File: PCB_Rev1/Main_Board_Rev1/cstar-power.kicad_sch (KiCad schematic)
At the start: 49 parts, among them IC1 LT8648SEV#PBF, J4 Conn_01x02_Pin, J5 XT60PW-M, J6 Conn_01x02_Pin, J7 Conn_01x02_Pin, J8 Conn_01x02_Pin, U1 AZ1117IH-3.3TRG1

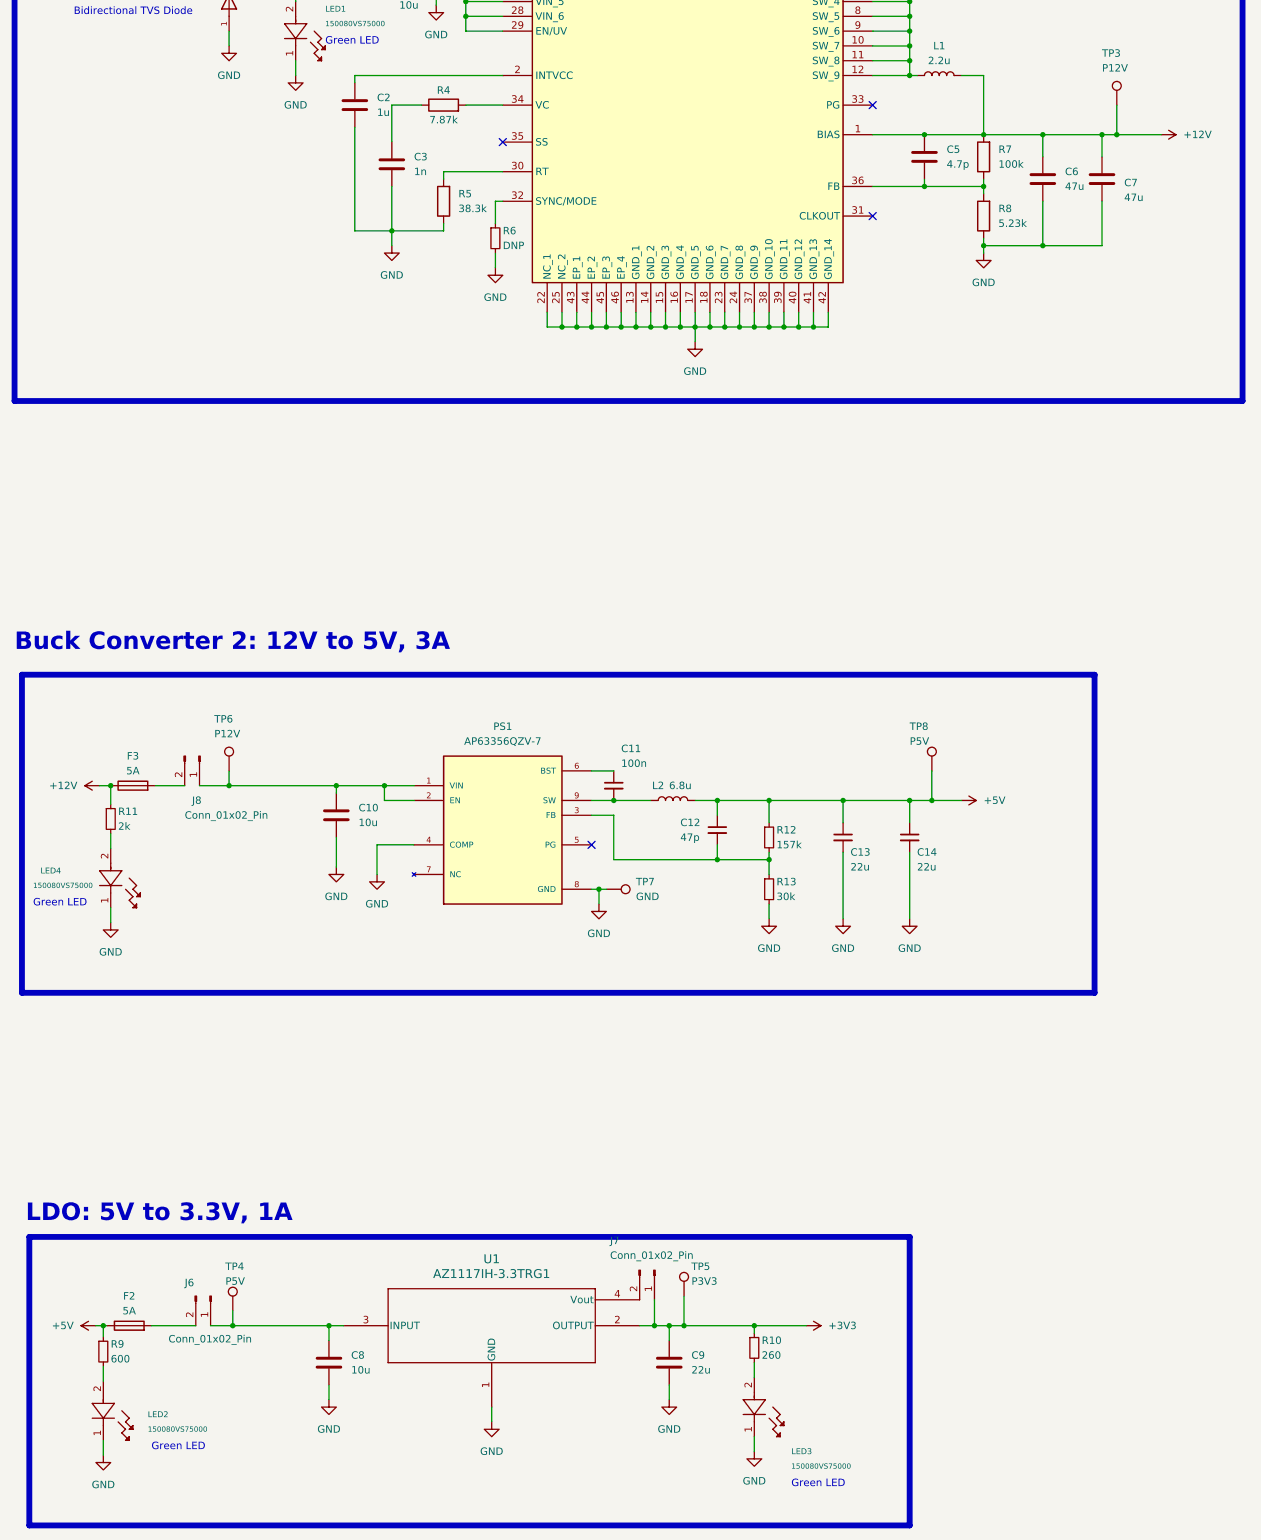
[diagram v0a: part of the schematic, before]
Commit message: schem changes made in BMS
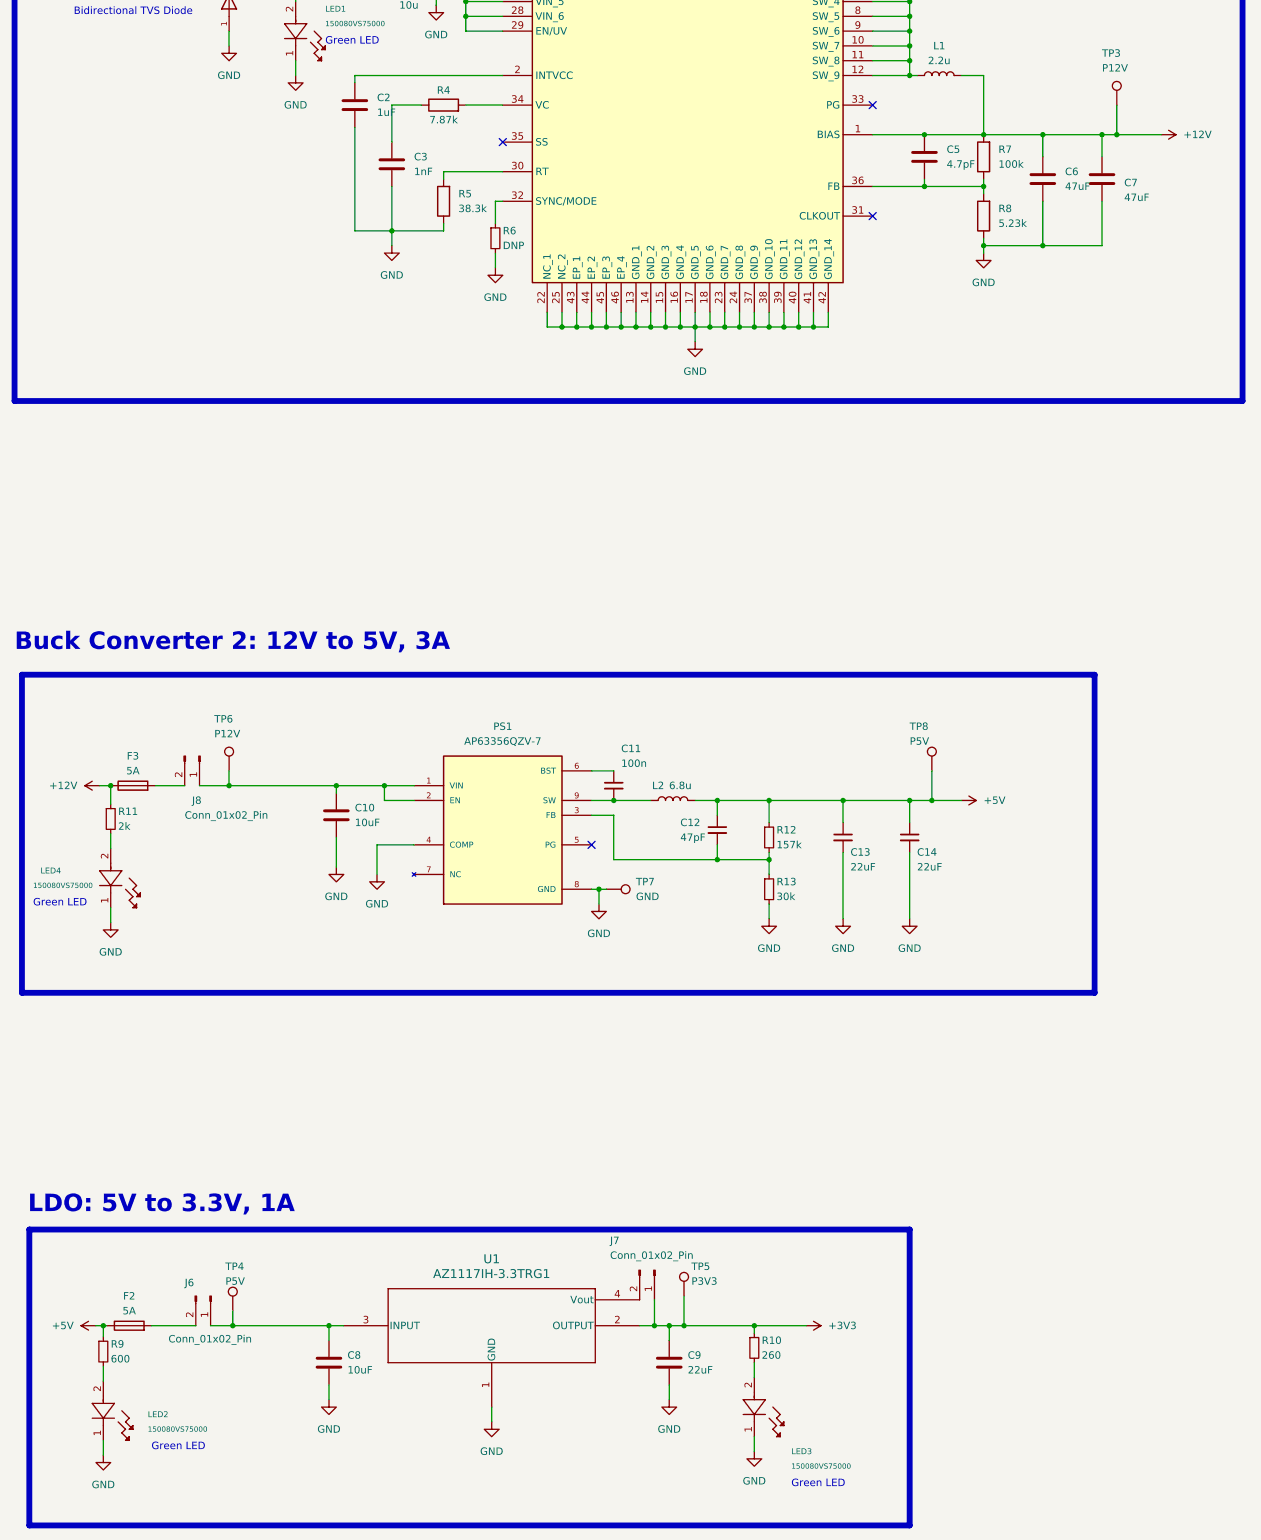
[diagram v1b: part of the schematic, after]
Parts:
- C10, C8: value 10u -> 10uF
- C12: value 47p -> 47pF
- C13, C14, C9: value 22u -> 22uF
- C2: value 1u -> 1uF
- C3: value 1n -> 1nF
- C5: value 4.7p -> 4.7pF
- C6, C7: value 47u -> 47uF
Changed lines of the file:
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@@
 	)
 	(rectangle
-		(start 45.72 292.1)
+		(start 45.72 290.83)
 		(end 196.85 341.63)
 		(stroke
@@
 	(text "LDO: 5V to 3.3V, 1A\n\n"
 		(exclude_from_sim no)
-		(at 45.085 294.64 0)
+		(at 45.466 293.116 0)
 		(effects
 			(font
@@
 			)
 		)
-		(property "Value" "47u"
+		(property "Value" "47uF"
 			(at 233.68 113.665 0)
 			(effects
@@
 		(fields_autoplaced yes)
 		(property "Reference" "C3"
-			(at 111.76 106.68 0)
+			(at 111.76 106.6799 0)
 			(effects
 				(font
@@
 			)
 		)
-		(property "Value" "1n"
-			(at 111.76 109.22 0)
+		(property "Value" "1nF"
+			(at 111.76 109.2199 0)
 			(effects
 				(font
@@
 		(fields_autoplaced yes)
 		(property "Reference" "C8"
-			(at 100.965 312.42 0)
+			(at 100.33 312.4199 0)
 			(effects
 				(font
@@
 			)
 		)
-		(property "Value" "10u"
-			(at 100.965 314.96 0)
+		(property "Value" "10uF"
+			(at 100.33 314.9599 0)
 			(effects
 				(font
@@
 			)
 		)
-		(property "Value" "47p"
+		(property "Value" "47pF"
 			(at 157.48 223.52 0)
 			(effects
@@
 		(fields_autoplaced yes)
 		(property "Reference" "C9"
-			(at 159.385 312.42 0)
+			(at 158.75 312.4199 0)
 			(effects
 				(font
@@
 			)
 		)
-		(property "Value" "22u"
-			(at 159.385 314.96 0)
+		(property "Value" "22uF"
+			(at 158.75 314.9599 0)
 			(effects
 				(font
@@
 		(fields_autoplaced yes)
 		(property "Reference" "C10"
-			(at 102.235 218.44 0)
+			(at 101.6 218.4399 0)
 			(effects
 				(font
@@
 			)
 		)
-		(property "Value" "10u"
-			(at 102.235 220.98 0)
+		(property "Value" "10uF"
+			(at 101.6 220.9799 0)
 			(effects
 				(font
@@
 			)
 		)
-		(property "Value" "22u"
+		(property "Value" "22uF"
 			(at 186.69 228.6 0)
 			(effects
@@
 			)
 		)
-		(property "Value" "22u"
+		(property "Value" "22uF"
 			(at 198.12 228.6 0)
 			(effects
@@
 			)
 		)
-		(property "Value" "1u"
+		(property "Value" "1uF"
 			(at 105.41 99.06 0)
 			(effects
@@
 		(fields_autoplaced yes)
 		(property "Reference" "C5"
-			(at 203.2 105.41 0)
+			(at 203.2 105.4099 0)
 			(effects
 				(font
@@
 			)
 		)
-		(property "Value" "4.7p"
-			(at 203.2 107.95 0)
+		(property "Value" "4.7pF"
+			(at 203.2 107.9499 0)
 			(effects
 				(font
@@
 		(fields_autoplaced yes)
 		(property "Reference" "C6"
-			(at 223.52 109.22 0)
+			(at 223.52 109.2199 0)
 			(effects
 				(font
@@
 			)
 		)
-		(property "Value" "47u"
-			(at 223.52 111.76 0)
+		(property "Value" "47uF"
+			(at 223.52 111.7599 0)
 			(effects
 				(font

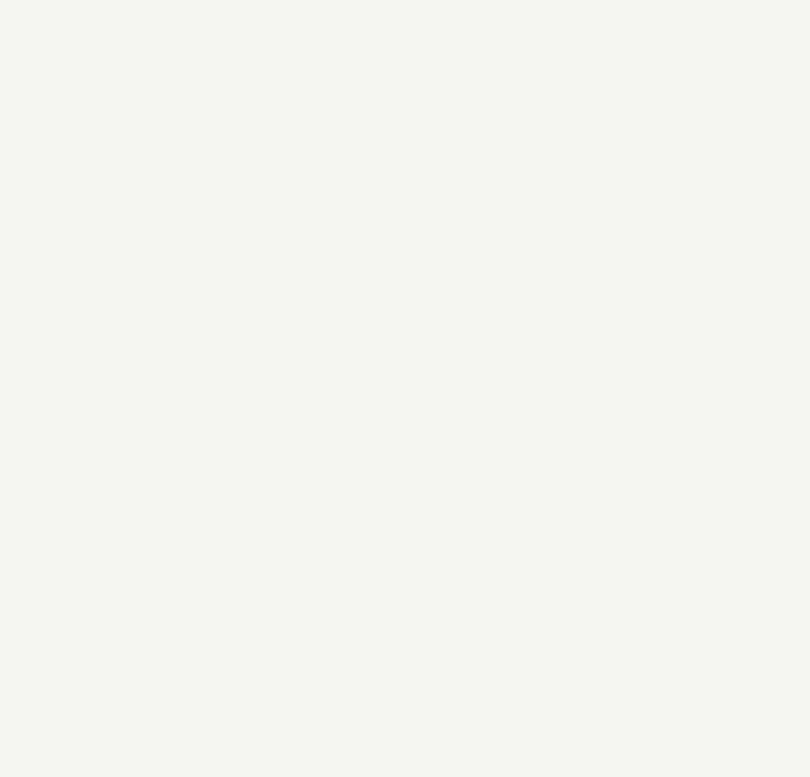
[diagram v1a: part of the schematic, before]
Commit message: Power nets (local + global) created
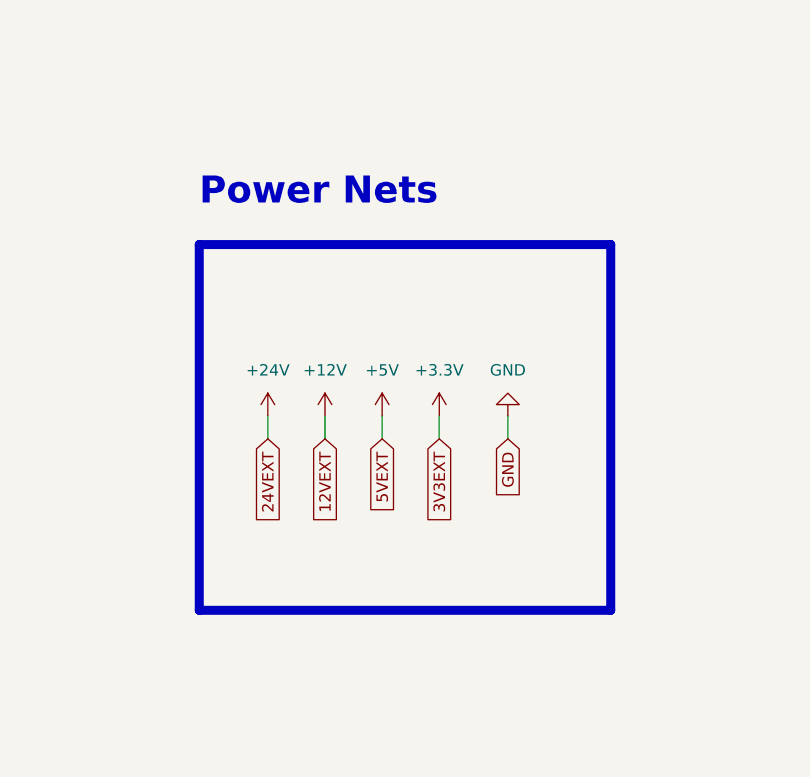
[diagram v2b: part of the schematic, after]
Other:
- note added: "Power Nets"

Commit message: deruioiygfhjik
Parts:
- added J14: USB4125-GF-A_REVA2, Footprints:GCT_USB4125-GF-A_REVA2, symbol USB:USB4125-GF-A_REVA2
- added R84, R85: 5.1k, Resistor_SMD:R_0805_2012Metric, symbol Device:R_Small
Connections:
- net +5V: now also J14.A9 (VBUS), J14.B9 (VBUS)
- net GND: now also J14.A12 (GND), J14.B12 (GND), J14.S1 (SHIELD), J14.S2 (SHIELD), J14.S3 (SHIELD), J14.S4 (SHIELD), R84.1, R85.1
- new net: J14.A5 (CC1), R85.2
- new net: J14.B5 (CC2), R84.2
